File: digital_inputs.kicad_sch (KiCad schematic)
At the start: 25 parts, among them J10 MMCX, J11 MMCX, J12 MMCX, J13 MMCX, J14 MMCX, J15 MMCX, J16 MMCX, J17 MMCX, J18 MMCX, J3 MMCX, J4 MMCX, J5 MMCX, J6 MMCX, J7 MMCX, J8 MMCX, J9 MMCX, U8 SN74LVC16244A-EP

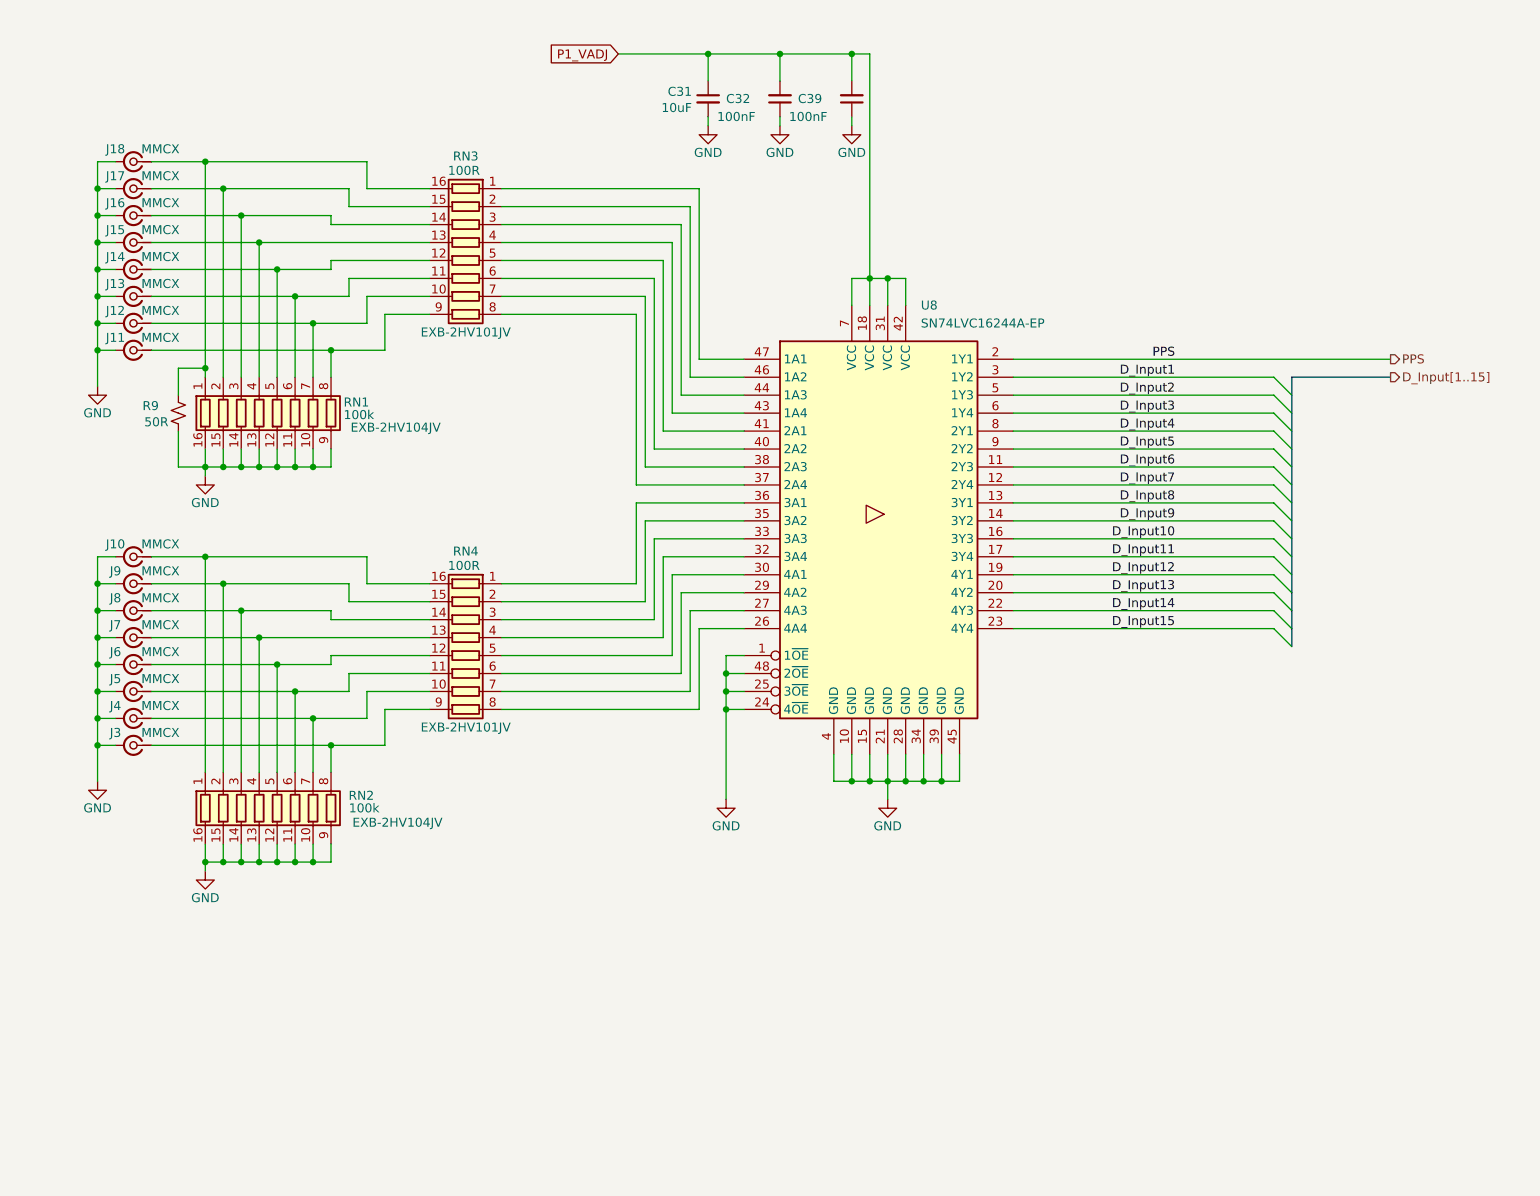
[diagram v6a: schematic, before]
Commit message: Changes to Based on Pre-Production Run
- Added FPGA control for digital input buffer's OE pin with pull up
- Grounded ref caps on ADC properly
- Swapped pins 5&6 on U7 (polarity fix)
- Fixed naming of CLK inputs to be  "CLK1" / "CLK2" to be clk0 & clk1 inputs on LMK
    - Changed "J" tag to be digital IO only "J1 - J16"
- Mounting Holes changed 3.0mm to match with Marble
- Added 50ohm non-populated resistors in on digital inputs

- Changed labeling of ADC inputs in schematic (no copper changes)
- Changed labeling/assignment of digital inputs on the FMC connector (almost no copper changes)
	- now J1 = Dinput1 ... J15= Dinput16; J16 = PPS (PPS has unchanged mapping)
- Swapped h37 and g37 pin assignments (new D15 &D14)
	- for better compatibility with new FMC template

These changes were covered by moving to the new FMC template:
- Add heartbeat LED
- Add SN on both sides
- Move SN and logo to template side of board
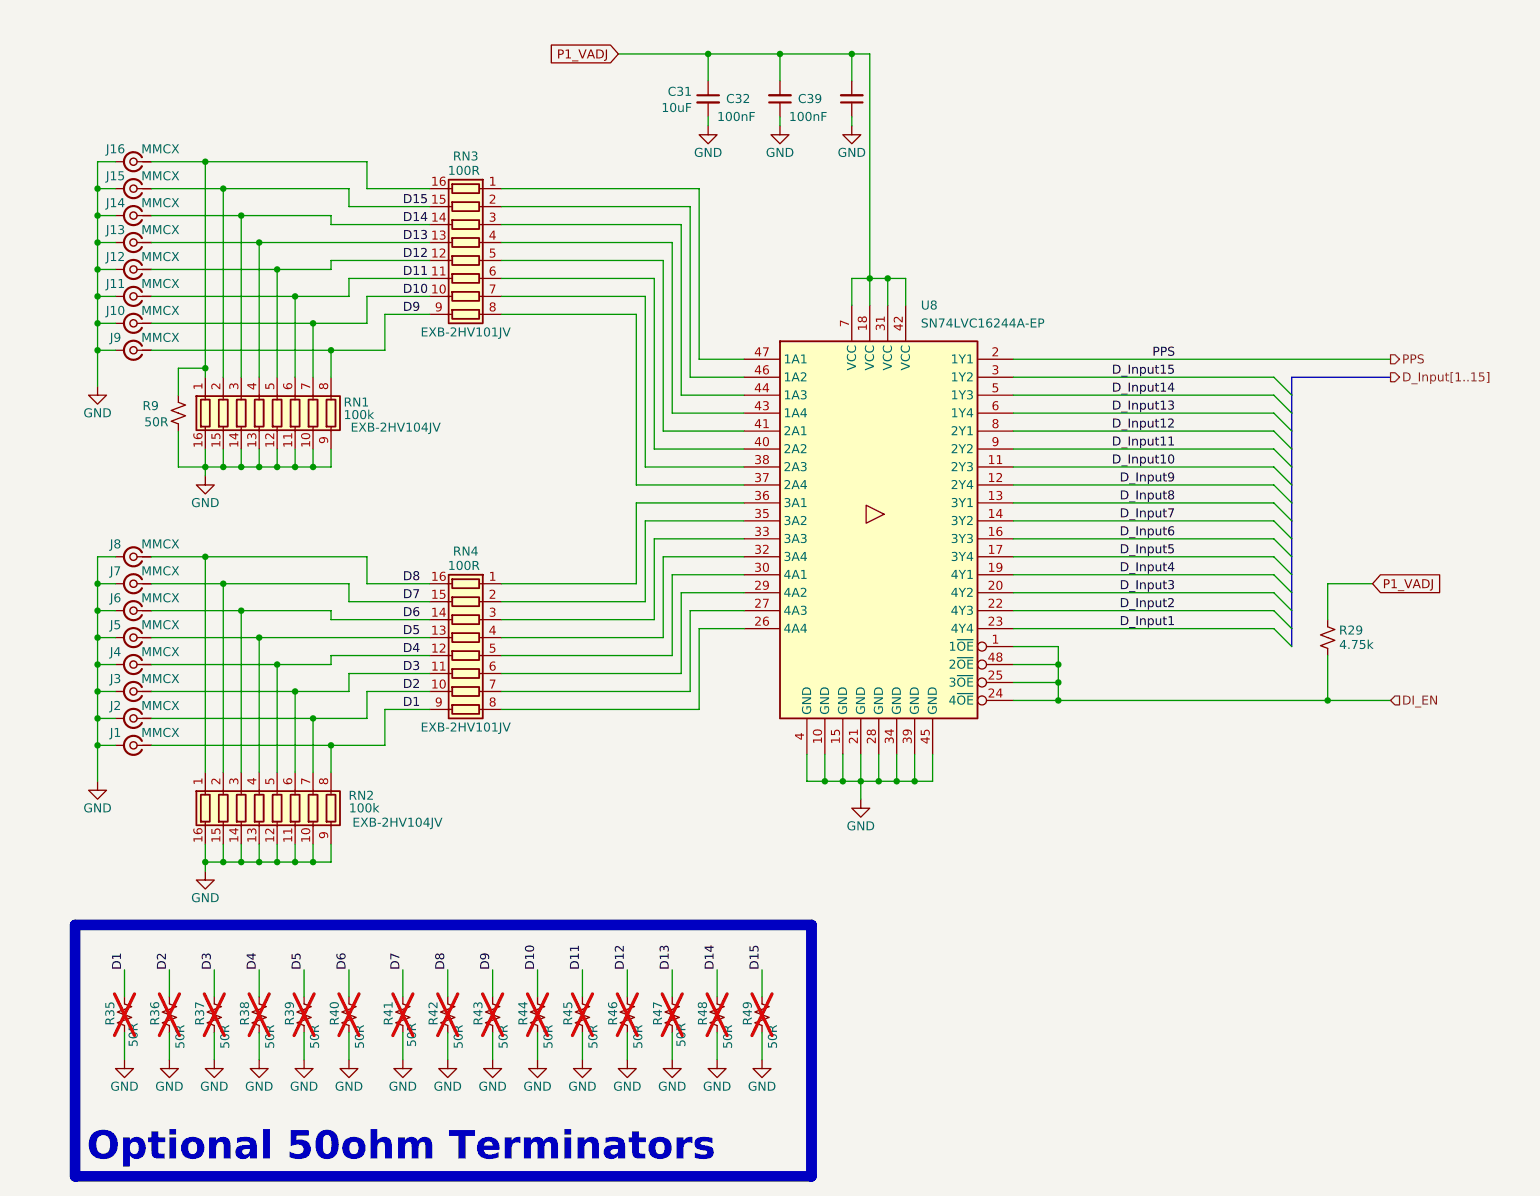
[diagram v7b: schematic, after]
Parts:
- added R29: 4.75k, Resistor_SMD:R_0603_1608Metric, symbol Device:R_Small_US
- added R35, R36, R37, R38, R39, R40, R41, R42, R43, R44, R45, R46, R47, R48, R49: 50R, Resistor_SMD:R_1206_3216Metric, symbol Device:R_Small_US
- renumbered J3 to J1, J12 to J10, J13 to J11, J14 to J12, J15 to J13, J16 to J14, J17 to J15, J18 to J16, J4 to J2, J5 to J3, J6 to J4, J7 to J5, J8 to J6, J9 to J7, J10 to J8, J11 to J9
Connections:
- net D_Input1: now also U8.23 (4Y4); no longer U8.3 (1Y2)
- net D_Input10: now also U8.11 (2Y3); no longer U8.16 (3Y3)
- net D_Input11: now also U8.9 (2Y2); no longer U8.17 (3Y4)
- net D_Input12: now also U8.8 (2Y1); no longer U8.19 (4Y1)
- net D_Input13: now also U8.6 (1Y4); no longer U8.20 (4Y2)
- net D_Input14: now also U8.5 (1Y3); no longer U8.22 (4Y3)
- net D_Input15: now also U8.3 (1Y2); no longer U8.23 (4Y4)
- net D_Input2: now also U8.22 (4Y3); no longer U8.5 (1Y3)
- net D_Input3: now also U8.20 (4Y2); no longer U8.6 (1Y4)
- net D_Input4: now also U8.19 (4Y1); no longer U8.8 (2Y1)
- net D_Input5: now also U8.17 (3Y4); no longer U8.9 (2Y2)
- net D_Input6: now also U8.16 (3Y3); no longer U8.11 (2Y3)
- net D_Input7: now also U8.14 (3Y2); no longer U8.12 (2Y4)
- net D_Input9: now also U8.12 (2Y4); no longer U8.14 (3Y2)
- net GND: now also R35.2, R36.2, R37.2, R38.2, R39.2, R40.2, R41.2, R42.2, R43.2, R44.2, R45.2, R46.2, R47.2, R48.2, R49.2; no longer U8.1 (1~{OE}), U8.24 (4~{OE}), U8.25 (3~{OE}), U8.48 (2~{OE})
- net P1_VADJ: now also R29.2
- net D3: now reaches J3.1 (In), RN2.6 (R6.1), RN4.11 (R6.2)
- net D3: now also R37.1
- net D6: now reaches J6.1 (In), RN2.3 (R3.1), RN4.14 (R3.2)
- net D6: now also R40.1
- net D8: now reaches J8.1 (In), RN2.1 (R1.1), RN4.16 (R1.2)
- net D8: now also R42.1
- net D7: now reaches J7.1 (In), RN2.2 (R2.1), RN4.15 (R2.2)
- net D7: now also R41.1
- net D5: now reaches J5.1 (In), RN2.4 (R4.1), RN4.13 (R4.2)
- net D5: now also R39.1
- net D4: now reaches J4.1 (In), RN2.5 (R5.1), RN4.12 (R5.2)
- net D4: now also R38.1
- net D2: now reaches J2.1 (In), RN2.7 (R7.1), RN4.10 (R7.2)
- net D2: now also R36.1
- net D1: now reaches J1.1 (In), RN2.8 (R8.1), RN4.9 (R8.2)
- net D1: now also R35.1
- net D9: now reaches J9.1 (In), RN1.8 (R8.1), RN3.9 (R8.2)
- net D9: now also R43.1
- net D10: now reaches J10.1 (In), RN1.7 (R7.1), RN3.10 (R7.2)
- net D10: now also R44.1
- net D11: now reaches J11.1 (In), RN1.6 (R6.1), RN3.11 (R6.2)
- net D11: now also R45.1
- net D15: now reaches J15.1 (In), RN1.2 (R2.1), RN3.15 (R2.2)
- net D15: now also R49.1
- net D14: now reaches J14.1 (In), RN1.3 (R3.1), RN3.14 (R3.2)
- net D14: now also R48.1
- net D13: now reaches J13.1 (In), RN1.4 (R4.1), RN3.13 (R4.2)
- net D13: now also R47.1
- net D12: now reaches J12.1 (In), RN1.5 (R5.1), RN3.12 (R5.2)
- net D12: now also R46.1
- new net DI_EN: R29.1, U8.1 (1~{OE}), U8.24 (4~{OE}), U8.25 (3~{OE}), U8.48 (2~{OE})
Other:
- note added: "Optional 50ohm Terminators"

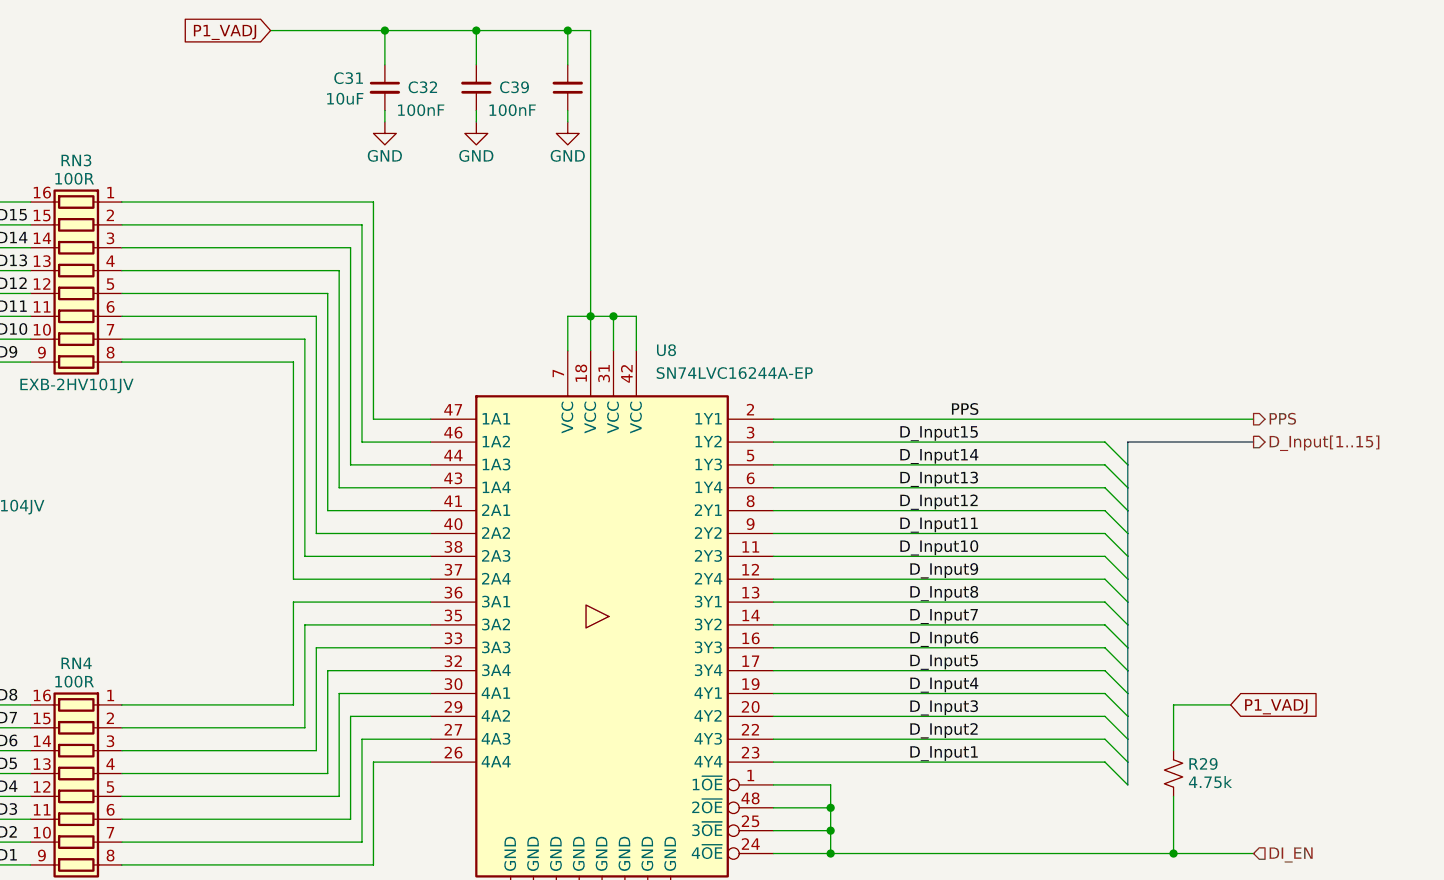
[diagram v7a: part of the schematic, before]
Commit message: Updates based on Review
-Added Missing "PG_C2M" label
-Added heartbeat signal to fmc (was missing on previous commit)
-Changed all vias to 0.6mm with 0.3mm hole
	-Adjusted one via near pin7 of U7 to accommodate this change
-Changed traces around U4 to R25 to keep trace straight
-Added GND via at pin5 of U7 & connected all GND pins of U7 to PAD
-Moved R9 near J16 connector
-Changed name of board on silkscreen to "Clock Input FMC" project/file name changes will come in later commits.
-Standardized "J*" labels to all be consistent
-Swapped FMC pins for Din14 & Din15. This undoes some complications in the last commit with pin swaps
-Removed net references to "P1_" in net names
-Adjusted plane layers keepout and min width to be more consistent
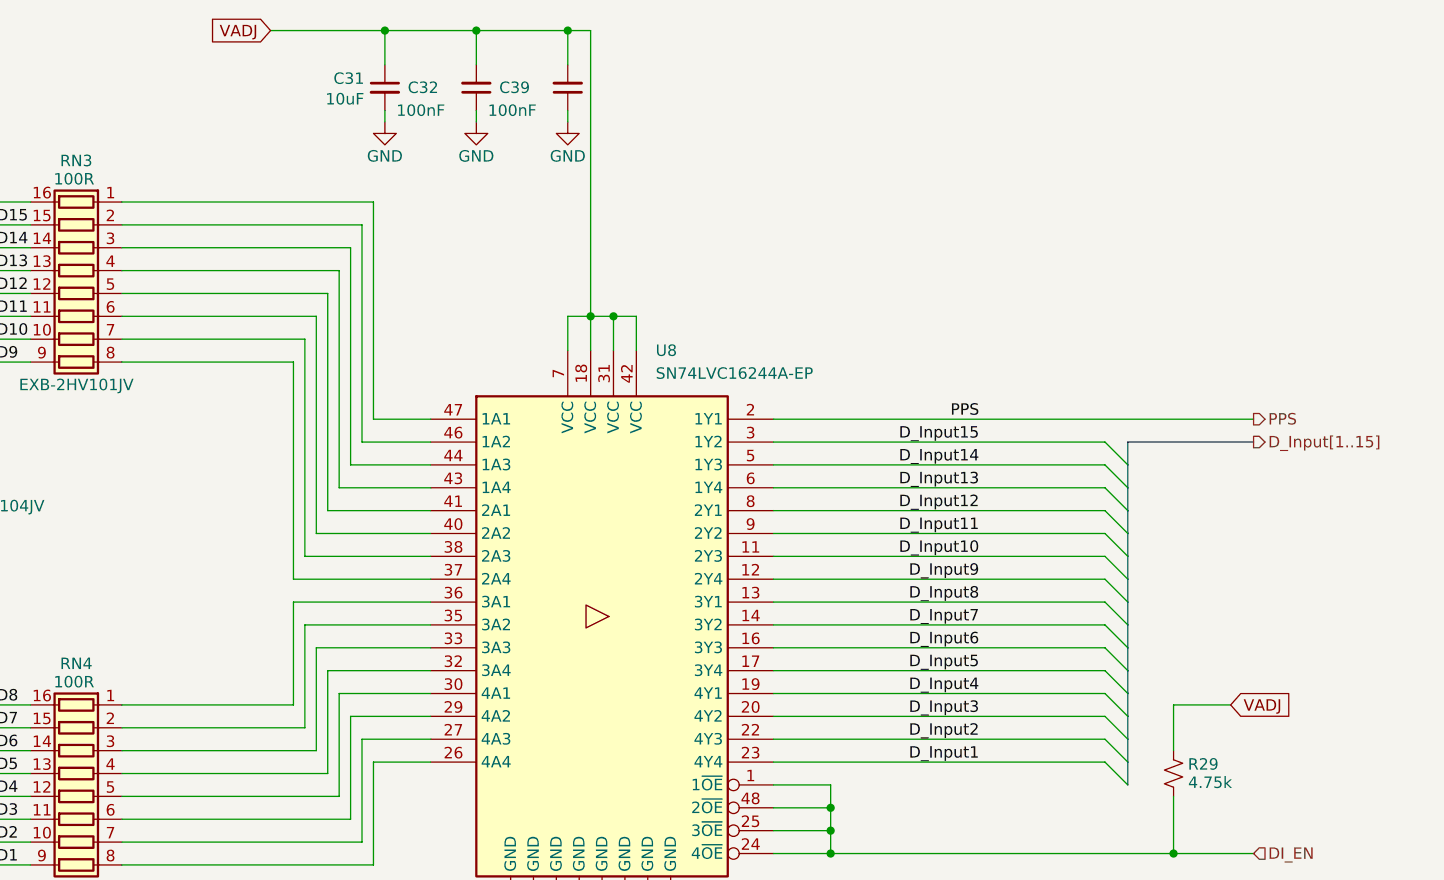
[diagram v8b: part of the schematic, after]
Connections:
- net P1_VADJ renamed VADJ
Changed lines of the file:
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@@
 		)
 	)
-	(global_label "P1_VADJ"
+	(global_label "VADJ"
 		(shape input)
 		(at 220.98 116.84 0)
@@
 		)
 		(property "Intersheetrefs" "${INTERSHEET_REFS}"
-			(at 231.8271 116.84 0)
+			(at 228.38 116.84 0)
 			(effects
 				(font
@@
 		)
 	)
-	(global_label "P1_VADJ"
+	(global_label "VADJ"
 		(shape input)
 		(at 114.3 41.91 180)
@@
 		)
 		(property "Intersheetrefs" "${INTERSHEET_REFS}"
-			(at 103.4529 41.91 0)
+			(at 106.9 41.91 0)
 			(effects
 				(font
